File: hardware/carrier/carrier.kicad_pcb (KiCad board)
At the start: 2 copper layers, 117.9 x 72.3 mm, 15 parts, among them J1 12V in, U1 D1 Mini ESP32 (Type-C), U2 PCA9685 16ch servo, U3 LM2596 buck 12V->5.05V

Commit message: carrier: J1 turned to face the back of the box, D1 model without sockets
Scott's review of the 3D view: the terminal block's wire entry faced the
board edge it sat against, and the D1 Mini sat on female sockets it will
not have. J1 moves below the buck at (50.5,14.5) rot 180 so the entry faces
the PCA edge (the back of the box) and the wires leave over the chamfer;
TP5 moves to (54,7.5) out from under it. Rejected: keeping J1 on the right
edge turned 180 - its body then overlaps the LM2596 courtyard unless pushed
to 0.2 mm from the edge. +12V rerouted J1.1 -> north -> TP1 with the y=2
run teeing off; J1 GND made solid (full return current, same as IN-).
D1: ratgdo's STEP with the socket SHAPE_REPRESENTATION_RELATIONSHIP line
removed rather than a hand-built model - keeps ratgdo's tuned frame; the
socketed original is dropped from the tree (32 MB, in history).
DRC 0/0/0, pour 1 polygon + the known sliver, gerbers/drill re-exported,
pcbmill consolidate exact + annulus gate passed.

Co-Authored-By: Claude Fable 5.1 <noreply@anthropic.com>
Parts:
- moved J1 12.5 mm to (150.5, 114.5), turned to 180 degrees
- moved TP5 6.95 mm to (154.0, 107.5)
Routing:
- net +12V: track 38.2 -> 50.7 mm
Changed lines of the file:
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@@
 		)
 		(embedded_fonts no)
-		(model "${KIPRJMOD}/3dmodels/D1_Mini_ESP32.stp"
+		(model "${KIPRJMOD}/3dmodels/D1_Mini_ESP32_male.stp"
 			(offset
-				(xyz -0.5 -0.5 0)
+				(xyz -0.5 -0.5 -8.5)
 			)
 			(scale
@@
 	(footprint "carrier:TestPoint_THT_D2.2_1.181"
 		(layer "F.Cu")
-		(at 150.5 113.5)
+		(at 154 107.5)
 		(descr "Drilled test point, 2.2 pad on the 1.181 bit (0.51 annulus)")
 		(property "Reference" "TP5"
@@
 	(footprint "carrier:KF301_1x02_P5.08"
 		(layer "F.Cu")
-		(at 150.5 102 -90)
+		(at 150.5 114.5 180)
 		(descr "KF301-5.0 screw terminal 2P 5.08 mm, pads 2.6/1.181")
 		(property "Reference" "J1"
-			(at 2.54 -2.4 270)
+			(at 2.54 -2.4 180)
 			(layer "F.SilkS")
 			(effects
@@
 		)
 		(property "Value" "12V in"
-			(at 2.54 0 270)
+			(at 2.54 0 180)
 			(layer "F.Fab")
 			(effects
@@
 		)
 		(property "Datasheet" ""
-			(at 0 0 270)
+			(at 0 0 180)
 			(layer "F.Fab")
 			(hide yes)
@@
 		)
 		(property "Description" "KF301-5.0 screw terminal 2P 5.08 mm, pads 2.6/1.181"
-			(at 0 0 270)
+			(at 0 0 180)
 			(layer "F.Fab")
 			(hide yes)
@@
 		(duplicate_pad_numbers_are_jumpers no)
 		(fp_line
+			(start 7.62 3.5)
+			(end -2.54 3.5)
+			(stroke
+				(width 0.12)
+				(type solid)
+			)
+			(layer "F.SilkS")
+		)
+		(fp_line
+			(start 7.62 -4.1)
+			(end 7.62 3.5)
+			(stroke
+				(width 0.12)
+				(type solid)
+			)
+			(layer "F.SilkS")
+		)
+		(fp_line
 			(start -2.54 3.5)
 			(end -2.54 -4.1)
@@
 		)
 		(fp_line
+			(start -2.54 -4.1)
+			(end 7.62 -4.1)
+			(stroke
+				(width 0.12)
+				(type solid)
+			)
+			(layer "F.SilkS")
+		)
+		(fp_line
+			(start 7.9 3.8)
+			(end -2.8 3.8)
+			(stroke
+				(width 0.05)
+				(type solid)
+			)
+			(layer "F.CrtYd")
+		)
+		(fp_line
+			(start 7.9 -4.4)
+			(end 7.9 3.8)
+			(stroke
+				(width 0.05)
+				(type solid)
+			)
+			(layer "F.CrtYd")
+		)
+		(fp_line
+			(start -2.8 3.8)
+			(end -2.8 -4.4)
+			(stroke
+				(width 0.05)
+				(type solid)
+			)
+			(layer "F.CrtYd")
+		)
+		(fp_line
+			(start -2.8 -4.4)
+			(end 7.9 -4.4)
+			(stroke
+				(width 0.05)
+				(type solid)
+			)
+			(layer "F.CrtYd")
+		)
+		(fp_line
 			(start 7.62 3.5)
 			(end -2.54 3.5)
 			(stroke
-				(width 0.12)
-				(type solid)
-			)
-			(layer "F.SilkS")
+				(width 0.1)
+				(type solid)
+			)
+			(layer "F.Fab")
+		)
+		(fp_line
+			(start 7.62 -4.1)
+			(end 7.62 3.5)
+			(stroke
+				(width 0.1)
+				(type solid)
+			)
+			(layer "F.Fab")
+		)
+		(fp_line
+			(start -2.54 3.5)
+			(end -2.54 -4.1)
+			(stroke
+				(width 0.1)
+				(type solid)
+			)
+			(layer "F.Fab")
 		)
 		(fp_line
@@
 			(end 7.62 -4.1)
 			(stroke
-				(width 0.12)
-				(type solid)
-			)
-			(layer "F.SilkS")
-		)
-		(fp_line
-			(start 7.62 -4.1)
-			(end 7.62 3.5)
-			(stroke
-				(width 0.12)
-				(type solid)
-			)
-			(layer "F.SilkS")
-		)
-		(fp_line
-			(start -2.8 3.8)
-			(end -2.8 -4.4)
-			(stroke
-				(width 0.05)
-				(type solid)
-			)
-			(layer "F.CrtYd")
-		)
-		(fp_line
-			(start 7.9 3.8)
-			(end -2.8 3.8)
-			(stroke
-				(width 0.05)
-				(type solid)
-			)
-			(layer "F.CrtYd")
-		)
-		(fp_line
-			(start -2.8 -4.4)
-			(end 7.9 -4.4)
-			(stroke
-				(width 0.05)
-				(type solid)
-			)
-			(layer "F.CrtYd")
-		)
-		(fp_line
-			(start 7.9 -4.4)
-			(end 7.9 3.8)
-			(stroke
-				(width 0.05)
-				(type solid)
-			)
-			(layer "F.CrtYd")
-		)
-		(fp_line
-			(start -2.54 3.5)
-			(end -2.54 -4.1)
-			(stroke
 				(width 0.1)
 				(type solid)
@@
 			(layer "F.Fab")
 		)
-		(fp_line
-			(start 7.62 3.5)
-			(end -2.54 3.5)
-			(stroke
-				(width 0.1)
-				(type solid)
-			)
-			(layer "F.Fab")
-		)
-		(fp_line
-			(start -2.54 -4.1)
-			(end 7.62 -4.1)
-			(stroke
-				(width 0.1)
-				(type solid)
-			)
-			(layer "F.Fab")
-		)
-		(fp_line
-			(start 7.62 -4.1)
-			(end 7.62 3.5)
-			(stroke
-				(width 0.1)
-				(type solid)
-			)
-			(layer "F.Fab")
+		(fp_text user "GND"
+			(at 5.08 2.4 180)
+			(layer "F.SilkS")
+			(effects
+				(font
+					(size 0.8 0.8)
+					(thickness 0.15)
+				)
+			)
 		)
 		(fp_text user "12V"
-			(at 0 2.4 270)
-			(layer "F.SilkS")
-			(effects
-				(font
-					(size 0.8 0.8)
-					(thickness 0.15)
-				)
-			)
-		)
-		(fp_text user "GND"
-			(at 5.08 2.4 270)
+			(at 0 2.4 180)
 			(layer "F.SilkS")
 			(effects
@@
 		)
 		(pad "1" thru_hole rect
-			(at 0 0 270)
+			(at 0 0 180)
 			(size 2.6 2.6)
 			(drill 1.181)
@@
 		)
 		(pad "2" thru_hole circle
-			(at 5.08 0 270)
+			(at 5.08 0 180)
 			(size 2.6 2.6)
 			(drill 1.181)
@@
 			(remove_unused_layers no)
 			(net "GND")
+			(zone_connect 2)
 			(thermal_bridge_angle 90)
 		)
@@
 	)
 	(segment
-		(start 150.5 102)
+		(start 150.5 114.5)
 		(end 150.5 95)
 		(width 1)

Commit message: carrier: J1 at Scott's spot, C1 turned, schematic parity clean, STEP re-exported
Scott placed J1 at (45.05,15.7) between H4 and the chamfer after my move
left its body against the buck's IN- corner, and turned C1 so the TP2 stub
runs straight into it; that removes the diagonal and the pour sliver
(pour is one polygon). +12V goes east under J1 then north: straight north
from the new pad would graze IN- by 0.05.
The parity errors he saw were generator defects: NC pads without the
netlist's unconnected-() nets, symbol Description empty, Datasheet ~ vs
empty, and two different J1 values. Fixed at the source (gen_pcb/gen_sch)
rather than by excluding them in the .kicad_pro, so the check stays live.
docs STEP re-exported by kicad-cli after the rebuild - a GUI export from
before the rebuild was already stale.
ERC 0, DRC --schematic-parity 0/0/0, gerbers + drill re-exported, pcbmill
bit map exact + annulus gate passed.

Co-Authored-By: Claude Fable 5.1 <noreply@anthropic.com>
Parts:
- moved J1 5.58 mm to (145.1, 115.7)
- moved C1 2.93 mm to (60.2, 117.0), turned to 180 degrees
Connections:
- U1 pad 10: (no net) -> unconnected-(U1-IO19-Pad10)
- U1 pad 11: (no net) -> unconnected-(U1-IO34-Pad11)
- U1 pad 12: (no net) -> unconnected-(U1-IO23-Pad12)
- U1 pad 13: (no net) -> unconnected-(U1-IO14-Pad13)
- U1 pad 14: (no net) -> unconnected-(U1-IO5-Pad14)
- U1 pad 15: (no net) -> unconnected-(U1-NC-Pad15)
- U1 pad 18: (no net) -> unconnected-(U1-IO13-Pad18)
- U1 pad 2: (no net) -> unconnected-(U1-RST-Pad2)
- U1 pad 21: (no net) -> unconnected-(U1-TXD-Pad21)
- U1 pad 23: (no net) -> unconnected-(U1-RXD-Pad23)
- U1 pad 25: (no net) -> unconnected-(U1-SCL-Pad25)
- U1 pad 27: (no net) -> unconnected-(U1-SDA-Pad27)
- U1 pad 28: (no net) -> unconnected-(U1-IO32-Pad28)
- U1 pad 29: (no net) -> unconnected-(U1-IO17-Pad29)
- U1 pad 3: (no net) -> unconnected-(U1-NC-Pad3)
- U1 pad 30: (no net) -> unconnected-(U1-IO12-Pad30)
- U1 pad 31: (no net) -> unconnected-(U1-IO16-Pad31)
- U1 pad 32: (no net) -> unconnected-(U1-IO4-Pad32)
- U1 pad 34: (no net) -> unconnected-(U1-IO0-Pad34)
- U1 pad 36: (no net) -> unconnected-(U1-IO2-Pad36)
- U1 pad 4: (no net) -> unconnected-(U1-IO36-Pad4)
- U1 pad 5: (no net) -> unconnected-(U1-IO39-Pad5)
- U1 pad 6: (no net) -> unconnected-(U1-IO26-Pad6)
- U1 pad 7: (no net) -> unconnected-(U1-IO35-Pad7)
- U1 pad 8: (no net) -> unconnected-(U1-IO18-Pad8)
- U1 pad 9: (no net) -> unconnected-(U1-IO33-Pad9)
- U2 pad 10: (no net) -> unconnected-(U2-SCL-Pad10)
- U2 pad 11: (no net) -> unconnected-(U2-OE-Pad11)
- U2 pad 5: (no net) -> unconnected-(U2-OE-Pad5)
- U2 pad 8: (no net) -> unconnected-(U2-VCC-Pad8)
- U2 pad 9: (no net) -> unconnected-(U2-SDA-Pad9)
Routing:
- net +12V: track 50.7 -> 57.3 mm
- net +5V: track 240.5 -> 234.0 mm

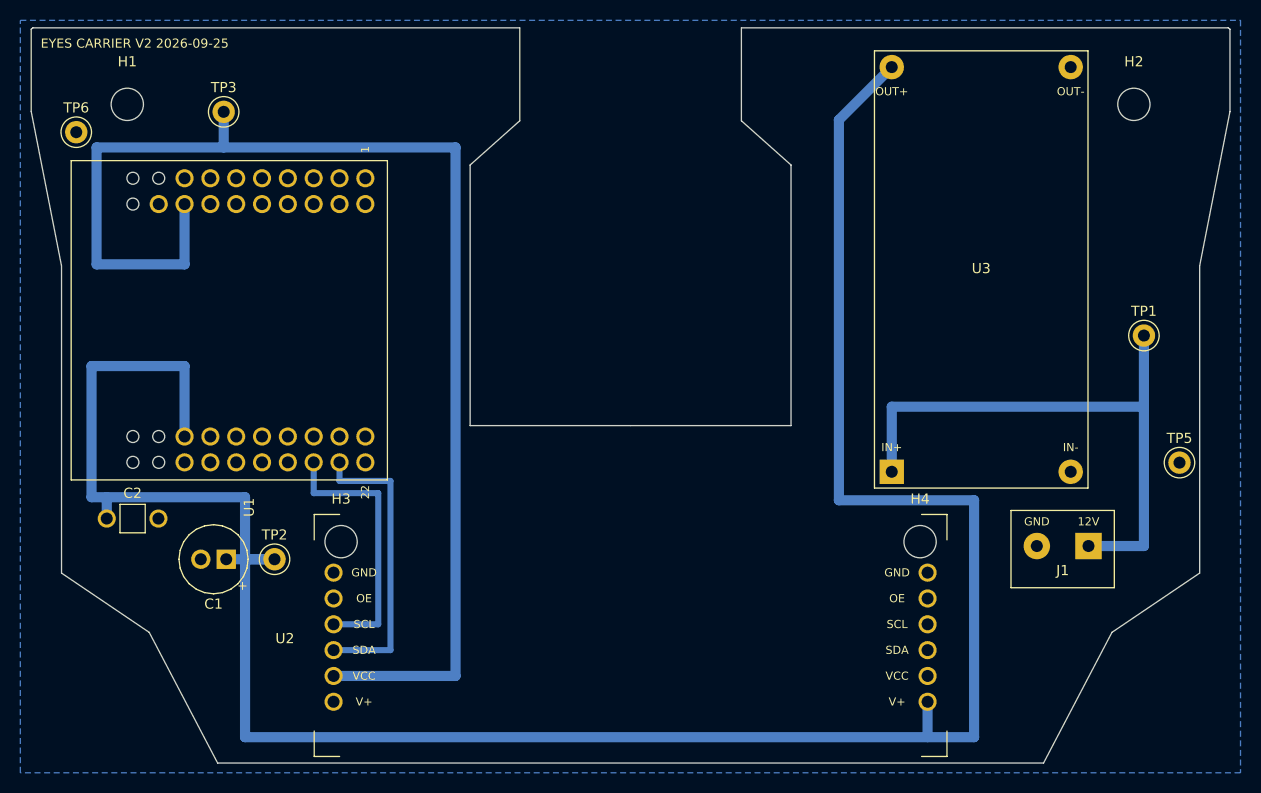
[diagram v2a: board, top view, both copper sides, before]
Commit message: carrier: back chamfers corner-to-corner (DXF kink was a cleanup error), silk text enlarged
The wood fit check against the case showed one straight chamfer where the
DXF had two segments; Scott confirmed the DXF was hand-edited after the
Fusion export. The two kink vertices are dropped from OUTLINE; outline.dxf
is no longer the master. Rejected re-exporting from Fusion: the case model
is not in this repo and the endpoints on the back edge and side matched the
case, so only the middle line was wrong.

Silk: refdes 1.0->1.2, labels 0.8->1.0, legend 0.9->1.2; LM2596 IN/OUT
labels moved 1.3 mm inward to clear the module outline. DRC+parity 0,
ERC 0, gerbers/drill/fit-check/STEP regenerated.

Co-Authored-By: Claude Fable 5.1 <noreply@anthropic.com>
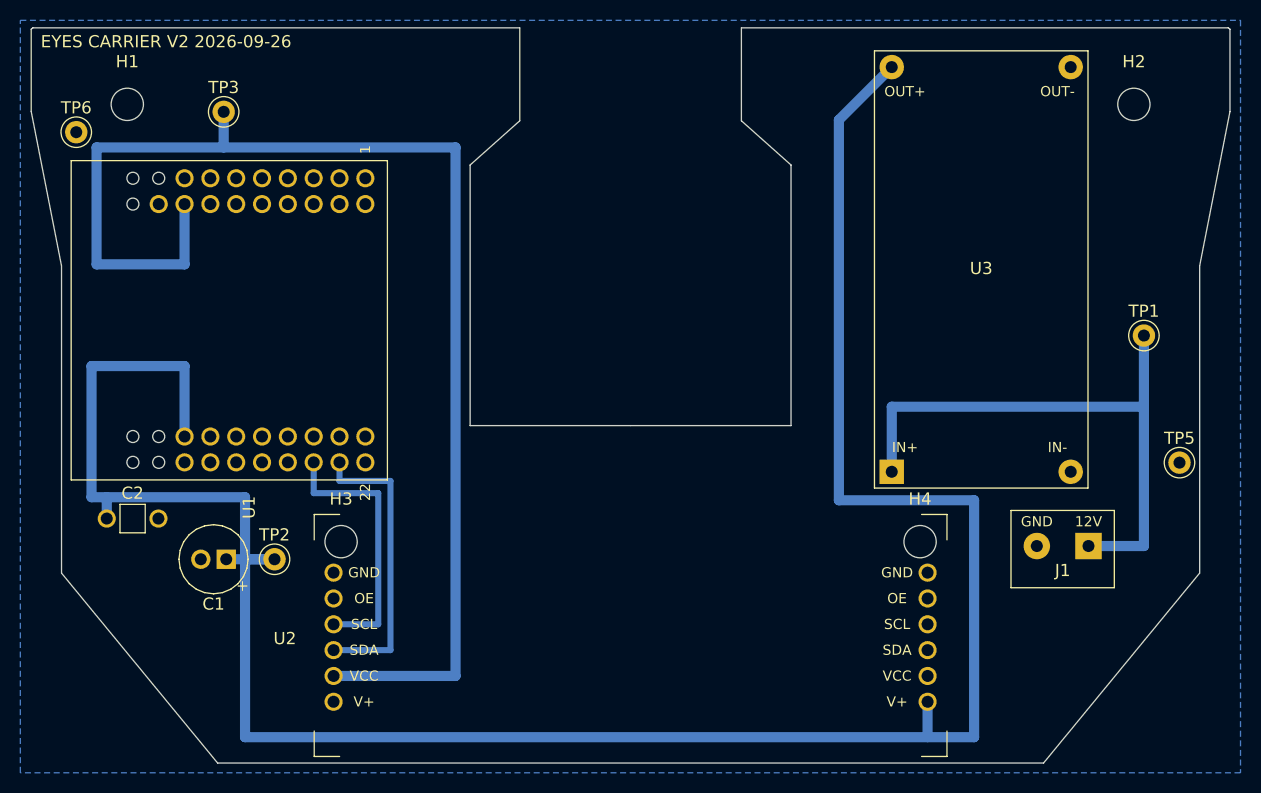
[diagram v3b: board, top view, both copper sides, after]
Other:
- outline, holes or cut-outs redrawn
- board text added: "EYES CARRIER V2 2026-09-26"
- board text removed: "EYES CARRIER V2 2026-09-25"

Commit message: carrier: back chamfers 4 mm deeper; two traces rerouted, no placement moved
Corner-to-corner still stuck out past the case panel at both back corners in
the wood check. Scott's estimate (not measured): bring each back corner in
about 4 mm. The chamfer is the corner-to-corner line offset 4 mm inward,
parallel: back-edge end -40.598 -> -35.420, side end 18.361 -> 12.061,
mirrored. Two caliper readings per corner would replace the estimate.

The new edge cut through two traces, so those moved and nothing else did:
- +5V trunk corner (-37.9, 34.5) is outside the deeper chamfer; it turns
  north at -33.8 now, then (-33.8, 18.2) -> TP2.
- +12V vertical 50.5 -> 47.5: the chamfer meeting the x=50.5 run pinched
  the pour to 0.1 mm between the right edge and the J1 pocket, and it
  poured as two islands (U2 pad 12 unconnected).

Rejected: moving TP5 to (54, -11) to free that pocket. It cleared the DRC
but moved Scott's placement to work around a trace of mine; moving the
trace keeps placement.py byte-identical and fixes the same pocket.
Rejected: pivoting only the back-edge endpoint (shallower cut) -- Scott's
photo shows the overhang along the whole chamfer, not just at the back.

DRC+parity 0/0/0, ERC 0, one pour polygon. Gerbers, fit-check SVG, STEP
regenerated. Drills unchanged.

Co-Authored-By: Claude Fable 5.1 <noreply@anthropic.com>
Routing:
- net +5V: track 234.0 -> 227.5 mm
- net +12V: track 57.3 -> 54.3 mm
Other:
- outline, holes or cut-outs redrawn
